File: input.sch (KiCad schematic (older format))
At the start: 15 parts

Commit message: Schematic finished
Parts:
- gave numbers to parts that had none: 15
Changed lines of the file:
@@
 LIBS:2450bl15b050
 LIBS:tlv4172
+LIBS:l4940d2t12-tr
+LIBS:tps54308
+LIBS:l78l33abu
+LIBS:adp150aujz-18
 LIBS:radar-cache
+LIBS:hn1c01fu
 EELAYER 25 0
 EELAYER END
 $Descr A4 11693 8268
 encoding utf-8
-Sheet 6 7
+Sheet 6 8
 Title ""
 Date ""
@@
 $EndDescr
 $Comp
-L 2500BP15M400 F?
+L 2500BP15M400 F601
 U 1 1 59D64427
 P 3330 3730
-F 0 "F?" H 3330 4180 60  0000 C CNN
+F 0 "F601" H 3330 4180 60  0000 C CNN
 F 1 "2500BP15M400" H 3830 3380 60  0000 C CNN
 F 2 "" H 3330 3730 60  0001 C CNN
@@
 $EndComp
 $Comp
-L taper T?
+L taper T601
 U 1 1 59D645E7
 P 2270 3730
-F 0 "T?" H 2270 3880 60  0000 C CNN
+F 0 "T601" H 2270 3880 60  0000 C CNN
 F 1 "taper" H 2170 3580 60  0000 C CNN
 F 2 "" H 2270 3730 60  0001 C CNN
@@
 $EndComp
 $Comp
-L GND #PWR?
+L GND #PWR056
 U 1 1 59D64760
 P 3360 4390
-F 0 "#PWR?" H 3360 4140 50  0001 C CNN
+F 0 "#PWR056" H 3360 4140 50  0001 C CNN
 F 1 "GND" H 3360 4240 50  0000 C CNN
 F 2 "" H 3360 4390 50  0001 C CNN
@@
 $EndComp
 $Comp
-L MGA-645T6 U?
+L MGA-645T6 U601
 U 1 1 59D64DB0
 P 5010 3730
-F 0 "U?" H 5010 4030 60  0000 C CNN
+F 0 "U601" H 5010 4030 60  0000 C CNN
 F 1 "MGA-645T6" H 5460 3380 60  0000 C CNN
 F 2 "" H 5010 3730 60  0001 C CNN
@@
 $EndComp
 $Comp
-L taper T?
+L taper T602
 U 1 1 59D651DD
 P 8520 3730
-F 0 "T?" H 8520 3880 60  0000 C CNN
+F 0 "T602" H 8520 3880 60  0000 C CNN
 F 1 "taper" H 8420 3580 60  0000 C CNN
 F 2 "" H 8520 3730 60  0001 C CNN
@@
 $EndComp
 $Comp
-L GND #PWR?
+L GND #PWR057
 U 1 1 59D653F1
 P 4910 4320
-F 0 "#PWR?" H 4910 4070 50  0001 C CNN
+F 0 "#PWR057" H 4910 4070 50  0001 C CNN
 F 1 "GND" H 4910 4170 50  0000 C CNN
 F 2 "" H 4910 4320 50  0001 C CNN
@@
 $EndComp
 $Comp
-L MGA-645T6 U?
+L MGA-645T6 U602
 U 1 1 59D659BC
 P 6900 3730
-F 0 "U?" H 6900 4030 60  0000 C CNN
+F 0 "U602" H 6900 4030 60  0000 C CNN
 F 1 "MGA-645T6" H 7350 3380 60  0000 C CNN
 F 2 "" H 6900 3730 60  0001 C CNN
@@
 $EndComp
 $Comp
-L GND #PWR?
+L GND #PWR058
 U 1 1 59D659C2
 P 6800 4320
-F 0 "#PWR?" H 6800 4070 50  0001 C CNN
+F 0 "#PWR058" H 6800 4070 50  0001 C CNN
 F 1 "GND" H 6800 4170 50  0000 C CNN
 F 2 "" H 6800 4320 50  0001 C CNN
@@
 RF_OUT
 $Comp
-L L_Small L?
+L L_Small L606
 U 1 1 59D6720C
 P 4240 4070
-F 0 "L?" H 4270 4110 50  0000 L CNN
+F 0 "L606" H 4270 4110 50  0000 L CNN
 F 1 "2.7n" H 4270 4030 50  0000 L CNN
 F 2 "" H 4240 4070 50  0001 C CNN
@@
 	2570 3730 2780 3730
 $Comp
-L L_Small L?
+L L_Small L605
 U 1 1 59D673E1
 P 6170 4050
-F 0 "L?" H 6200 4090 50  0000 L CNN
+F 0 "L605" H 6200 4090 50  0000 L CNN
 F 1 "2.7n" H 6200 4010 50  0000 L CNN
 F 2 "" H 6170 4050 50  0001 C CNN
@@
 $EndComp
 $Comp
-L L_Small L?
+L L_Small L603
 U 1 1 59D67473
 P 6020 3730
-F 0 "L?" H 6050 3770 50  0000 L CNN
+F 0 "L603" H 6050 3770 50  0000 L CNN
 F 1 "4.7n" H 6050 3690 50  0000 L CNN
 F 2 "" H 6020 3730 50  0001 C CNN
@@
 $EndComp
 $Comp
-L L_Small L?
+L L_Small L604
 U 1 1 59D67614
 P 7900 3730
-F 0 "L?" H 7930 3770 50  0000 L CNN
+F 0 "L604" H 7930 3770 50  0000 L CNN
 F 1 "4.7n" H 7930 3690 50  0000 L CNN
 F 2 "" H 7900 3730 50  0001 C CNN
@@
 Connection ~ 4240 3730
 $Comp
-L GND #PWR?
+L GND #PWR059
 U 1 1 59D67ABC
 P 4240 4360
-F 0 "#PWR?" H 4240 4110 50  0001 C CNN
+F 0 "#PWR059" H 4240 4110 50  0001 C CNN
 F 1 "GND" H 4240 4210 50  0000 C CNN
 F 2 "" H 4240 4360 50  0001 C CNN
@@
 	4240 4360 4240 4170
 $Comp
-L GND #PWR?
+L GND #PWR060
 U 1 1 59D67C59
 P 6170 4250
-F 0 "#PWR?" H 6170 4000 50  0001 C CNN
+F 0 "#PWR060" H 6170 4000 50  0001 C CNN
 F 1 "GND" H 6170 4100 50  0000 C CNN
 F 2 "" H 6170 4250 50  0001 C CNN
@@
 	6170 4150 6170 4250
 $Comp
-L +3V3 #PWR?
+L +3V3 #PWR061
 U 1 1 59D67FA5
 P 5210 2860
-F 0 "#PWR?" H 5210 2710 50  0001 C CNN
+F 0 "#PWR061" H 5210 2710 50  0001 C CNN
 F 1 "+3V3" H 5210 3000 50  0000 C CNN
 F 2 "" H 5210 2860 50  0001 C CNN
@@
 $EndComp
 $Comp
-L L_Small L?
+L L_Small L602
 U 1 1 59D67FDD
 P 5820 3220
-F 0 "L?" H 5850 3260 50  0000 L CNN
+F 0 "L602" H 5850 3260 50  0000 L CNN
 F 1 "3.9n" H 5850 3180 50  0000 L CNN
 F 2 "" H 5820 3220 50  0001 C CNN
@@
 $EndComp
 $Comp
-L L_Small L?
+L L_Small L601
 U 1 1 59D680B8
 P 7700 3210
-F 0 "L?" H 7730 3250 50  0000 L CNN
+F 0 "L601" H 7730 3250 50  0000 L CNN
 F 1 "3.9n" H 7730 3170 50  0000 L CNN
 F 2 "" H 7700 3210 50  0001 C CNN
@@
 	7700 3580 7700 3310
 $Comp
-L C_Small C?
+L C_Small C604
 U 1 1 59D6822A
 P 5450 3100
-F 0 "C?" H 5460 3170 50  0000 L CNN
+F 0 "C604" H 5460 3170 50  0000 L CNN
 F 1 "11p" H 5460 3020 50  0000 L CNN
 F 2 "" H 5450 3100 50  0001 C CNN
@@
 $EndComp
 $Comp
-L C_Small C?
+L C_Small C603
 U 1 1 59D68289
 P 5210 3100
-F 0 "C?" H 5220 3170 50  0000 L CNN
+F 0 "C603" H 5220 3170 50  0000 L CNN
 F 1 "0u1" H 5220 3020 50  0000 L CNN
 F 2 "" H 5210 3100 50  0001 C CNN
@@
 Connection ~ 5210 2910
 $Comp
-L +3V3 #PWR?
+L +3V3 #PWR062
 U 1 1 59D6867B
 P 7090 2830
-F 0 "#PWR?" H 7090 2680 50  0001 C CNN
+F 0 "#PWR062" H 7090 2680 50  0001 C CNN
 F 1 "+3V3" H 7090 2970 50  0000 C CNN
 F 2 "" H 7090 2830 50  0001 C CNN
@@
 $EndComp
 $Comp
-L C_Small C?
+L C_Small C602
 U 1 1 59D68681
 P 7330 3070
-F 0 "C?" H 7340 3140 50  0000 L CNN
+F 0 "C602" H 7340 3140 50  0000 L CNN
 F 1 "11p" H 7340 2990 50  0000 L CNN
 F 2 "" H 7330 3070 50  0001 C CNN
@@
 $EndComp
 $Comp
-L C_Small C?
+L C_Small C601
 U 1 1 59D68687
 P 7090 3070
-F 0 "C?" H 7100 3140 50  0000 L CNN
+F 0 "C601" H 7100 3140 50  0000 L CNN
 F 1 "0u1" H 7100 2990 50  0000 L CNN
 F 2 "" H 7090 3070 50  0001 C CNN
@@
 Connection ~ 5450 2910
 $Comp
-L GND #PWR?
+L GND #PWR063
 U 1 1 59D6874C
 P 5450 3270
-F 0 "#PWR?" H 5450 3020 50  0001 C CNN
+F 0 "#PWR063" H 5450 3020 50  0001 C CNN
 F 1 "GND" H 5450 3120 50  0000 C CNN
 F 2 "" H 5450 3270 50  0001 C CNN
@@
 $EndComp
 $Comp
-L GND #PWR?
+L GND #PWR064
 U 1 1 59D6878B
 P 7330 3270
-F 0 "#PWR?" H 7330 3020 50  0001 C CNN
+F 0 "#PWR064" H 7330 3020 50  0001 C CNN
 F 1 "GND" H 7330 3120 50  0000 C CNN
 F 2 "" H 7330 3270 50  0001 C CNN

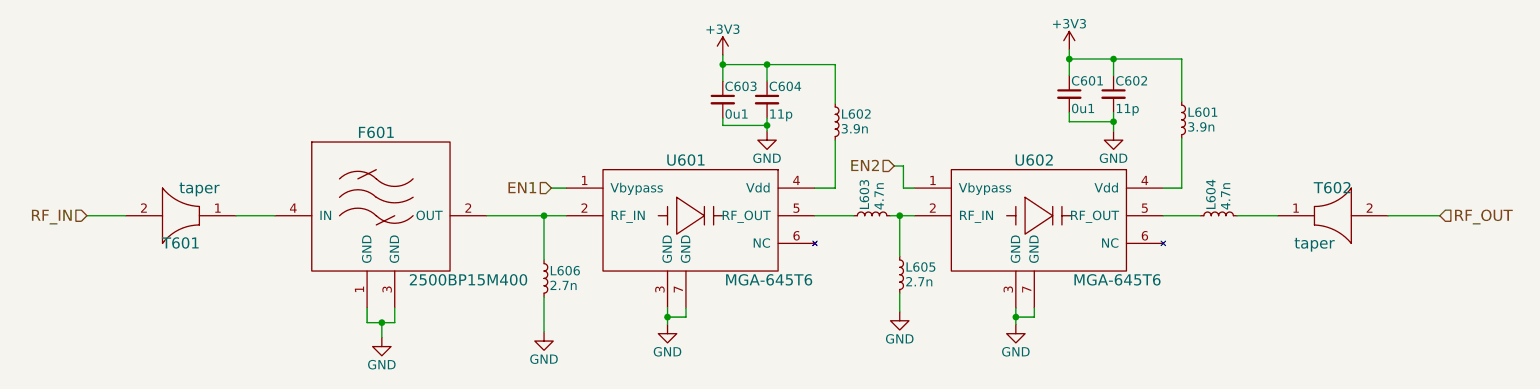
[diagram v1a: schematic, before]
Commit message: Assign a lot of footprints, fix l78l33abu part (input and output were reversed)
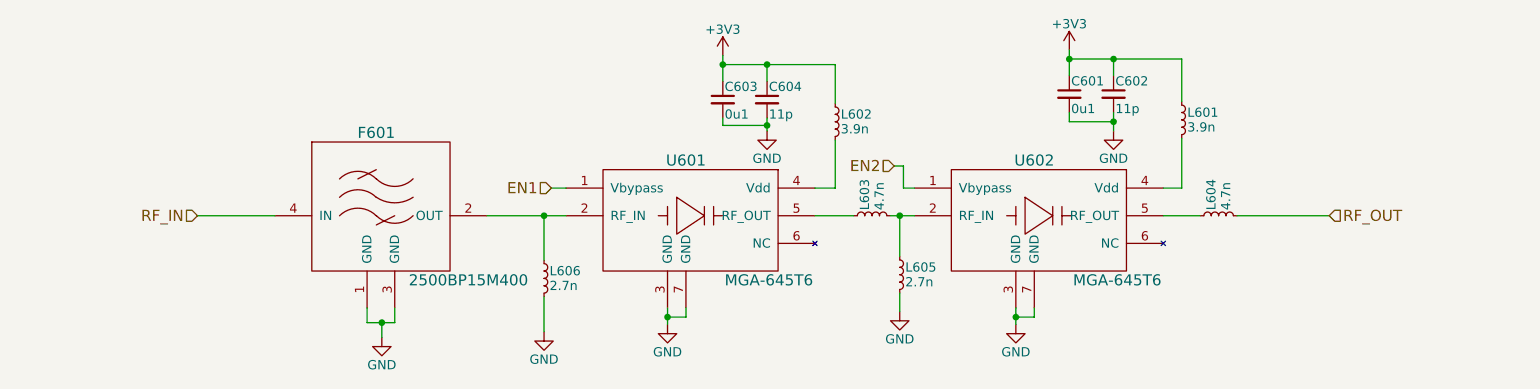
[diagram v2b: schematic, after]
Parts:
- removed T601, T602: taper, symbol taper
- C601, C603: footprint (none) -> Capacitors_SMD:C_0603_HandSoldering
- C602, C604, L601, L602, L603, L604, L605, L606: footprint (none) -> Capacitors_SMD:C_0402
- F601: footprint (none) -> rajsradar:2500BP15M400
- U601, U602: footprint (none) -> rajsradar:MGA-645T6
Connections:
- net RF_IN: now also F601.4 (IN)
- net RF_OUT: now also L604.2
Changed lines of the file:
@@
 F 0 "F601" H 3330 4180 60  0000 C CNN
 F 1 "2500BP15M400" H 3830 3380 60  0000 C CNN
-F 2 "" H 3330 3730 60  0001 C CNN
+F 2 "rajsradar:2500BP15M400" H 3330 3730 60  0001 C CNN
 F 3 "" H 3330 3730 60  0001 C CNN
 	1    3330 3730
@@
 $EndComp
 $Comp
-L taper T601
-U 1 1 59D645E7
-P 2270 3730
-F 0 "T601" H 2270 3880 60  0000 C CNN
-F 1 "taper" H 2170 3580 60  0000 C CNN
-F 2 "" H 2270 3730 60  0001 C CNN
-F 3 "" H 2270 3730 60  0001 C CNN
-	1    2270 3730
-	-1   0    0    1
-$EndComp
-$Comp
-L GND #PWR056
+L GND #PWR057
 U 1 1 59D64760
 P 3360 4390
-F 0 "#PWR056" H 3360 4140 50  0001 C CNN
+F 0 "#PWR057" H 3360 4140 50  0001 C CNN
 F 1 "GND" H 3360 4240 50  0000 C CNN
 F 2 "" H 3360 4390 50  0001 C CNN
@@
 F 0 "U601" H 5010 4030 60  0000 C CNN
 F 1 "MGA-645T6" H 5460 3380 60  0000 C CNN
-F 2 "" H 5010 3730 60  0001 C CNN
+F 2 "rajsradar:MGA-645T6" H 5010 3730 60  0001 C CNN
 F 3 "" H 5010 3730 60  0001 C CNN
 	1    5010 3730
@@
 $EndComp
 $Comp
-L taper T602
-U 1 1 59D651DD
-P 8520 3730
-F 0 "T602" H 8520 3880 60  0000 C CNN
-F 1 "taper" H 8420 3580 60  0000 C CNN
-F 2 "" H 8520 3730 60  0001 C CNN
-F 3 "" H 8520 3730 60  0001 C CNN
-	1    8520 3730
-	1    0    0    -1
-$EndComp
-$Comp
-L GND #PWR057
+L GND #PWR058
 U 1 1 59D653F1
 P 4910 4320
-F 0 "#PWR057" H 4910 4070 50  0001 C CNN
+F 0 "#PWR058" H 4910 4070 50  0001 C CNN
 F 1 "GND" H 4910 4170 50  0000 C CNN
 F 2 "" H 4910 4320 50  0001 C CNN
@@
 F 0 "U602" H 6900 4030 60  0000 C CNN
 F 1 "MGA-645T6" H 7350 3380 60  0000 C CNN
-F 2 "" H 6900 3730 60  0001 C CNN
+F 2 "rajsradar:MGA-645T6" H 6900 3730 60  0001 C CNN
 F 3 "" H 6900 3730 60  0001 C CNN
 	1    6900 3730
@@
 $EndComp
 $Comp
-L GND #PWR058
+L GND #PWR059
 U 1 1 59D659C2
 P 6800 4320
-F 0 "#PWR058" H 6800 4070 50  0001 C CNN
+F 0 "#PWR059" H 6800 4070 50  0001 C CNN
 F 1 "GND" H 6800 4170 50  0000 C CNN
 F 2 "" H 6800 4320 50  0001 C CNN
@@
 	1    0    0    -1
 $EndComp
-Text HLabel 1760 3730 0    60   Input ~ 0
+Text HLabel 2360 3730 0    60   Input ~ 0
 RF_IN
-Text HLabel 9100 3730 2    60   Input ~ 0
+Text HLabel 8500 3730 2    60   Input ~ 0
 RF_OUT
 $Comp
@@
 F 0 "L606" H 4270 4110 50  0000 L CNN
 F 1 "2.7n" H 4270 4030 50  0000 L CNN
-F 2 "" H 4240 4070 50  0001 C CNN
+F 2 "Capacitors_SMD:C_0402" H 4240 4070 50  0001 C CNN
 F 3 "" H 4240 4070 50  0001 C CNN
 	1    4240 4070
@@
 Connection ~ 6800 4280
 Wire Wire Line
-	9100 3730 8820 3730
-Wire Wire Line
-	1760 3730 1970 3730
-Wire Wire Line
-	2570 3730 2780 3730
+	8000 3730 8500 3730
+Wire Wire Line
+	2360 3730 2780 3730
 $Comp
 L L_Small L605
@@
 F 0 "L605" H 6200 4090 50  0000 L CNN
 F 1 "2.7n" H 6200 4010 50  0000 L CNN
-F 2 "" H 6170 4050 50  0001 C CNN
+F 2 "Capacitors_SMD:C_0402" H 6170 4050 50  0001 C CNN
 F 3 "" H 6170 4050 50  0001 C CNN
 	1    6170 4050
@@
 F 0 "L603" H 6050 3770 50  0000 L CNN
 F 1 "4.7n" H 6050 3690 50  0000 L CNN
-F 2 "" H 6020 3730 50  0001 C CNN
+F 2 "Capacitors_SMD:C_0402" H 6020 3730 50  0001 C CNN
 F 3 "" H 6020 3730 50  0001 C CNN
 	1    6020 3730
@@
 F 0 "L604" H 7930 3770 50  0000 L CNN
 F 1 "4.7n" H 7930 3690 50  0000 L CNN
-F 2 "" H 7900 3730 50  0001 C CNN
+F 2 "Capacitors_SMD:C_0402" H 7900 3730 50  0001 C CNN
 F 3 "" H 7900 3730 50  0001 C CNN
 	1    7900 3730
@@
 $EndComp
 Wire Wire Line
-	8000 3730 8220 3730
-Wire Wire Line
 	7800 3730 7600 3730
 Wire Wire Line
@@
 Connection ~ 4240 3730
 $Comp
-L GND #PWR059
+L GND #PWR060
 U 1 1 59D67ABC
 P 4240 4360
-F 0 "#PWR059" H 4240 4110 50  0001 C CNN
+F 0 "#PWR060" H 4240 4110 50  0001 C CNN
 F 1 "GND" H 4240 4210 50  0000 C CNN
 F 2 "" H 4240 4360 50  0001 C CNN
@@
 	4240 4360 4240 4170
 $Comp
-L GND #PWR060
+L GND #PWR061
 U 1 1 59D67C59
 P 6170 4250
-F 0 "#PWR060" H 6170 4000 50  0001 C CNN
+F 0 "#PWR061" H 6170 4000 50  0001 C CNN
 F 1 "GND" H 6170 4100 50  0000 C CNN
 F 2 "" H 6170 4250 50  0001 C CNN
@@
 	6170 4150 6170 4250
 $Comp
-L +3V3 #PWR061
+L +3V3 #PWR062
 U 1 1 59D67FA5
 P 5210 2860
-F 0 "#PWR061" H 5210 2710 50  0001 C CNN
+F 0 "#PWR062" H 5210 2710 50  0001 C CNN
 F 1 "+3V3" H 5210 3000 50  0000 C CNN
 F 2 "" H 5210 2860 50  0001 C CNN
@@
 F 0 "L602" H 5850 3260 50  0000 L CNN
 F 1 "3.9n" H 5850 3180 50  0000 L CNN
-F 2 "" H 5820 3220 50  0001 C CNN
+F 2 "Capacitors_SMD:C_0402" H 5820 3220 50  0001 C CNN
 F 3 "" H 5820 3220 50  0001 C CNN
 	1    5820 3220
@@
 F 0 "L601" H 7730 3250 50  0000 L CNN
 F 1 "3.9n" H 7730 3170 50  0000 L CNN
-F 2 "" H 7700 3210 50  0001 C CNN
+F 2 "Capacitors_SMD:C_0402" H 7700 3210 50  0001 C CNN
 F 3 "" H 7700 3210 50  0001 C CNN
 	1    7700 3210
@@
 F 0 "C604" H 5460 3170 50  0000 L CNN
 F 1 "11p" H 5460 3020 50  0000 L CNN
-F 2 "" H 5450 3100 50  0001 C CNN
+F 2 "Capacitors_SMD:C_0402" H 5450 3100 50  0001 C CNN
 F 3 "" H 5450 3100 50  0001 C CNN
 	1    5450 3100
@@
 F 0 "C603" H 5220 3170 50  0000 L CNN
 F 1 "0u1" H 5220 3020 50  0000 L CNN
-F 2 "" H 5210 3100 50  0001 C CNN
+F 2 "Capacitors_SMD:C_0603_HandSoldering" H 5210 3100 50  0001 C CNN
 F 3 "" H 5210 3100 50  0001 C CNN
 	1    5210 3100
@@
 Connection ~ 5210 2910
 $Comp
-L +3V3 #PWR062
+L +3V3 #PWR063
 U 1 1 59D6867B
 P 7090 2830
-F 0 "#PWR062" H 7090 2680 50  0001 C CNN
+F 0 "#PWR063" H 7090 2680 50  0001 C CNN
 F 1 "+3V3" H 7090 2970 50  0000 C CNN
 F 2 "" H 7090 2830 50  0001 C CNN
@@
 F 0 "C602" H 7340 3140 50  0000 L CNN
 F 1 "11p" H 7340 2990 50  0000 L CNN
-F 2 "" H 7330 3070 50  0001 C CNN
+F 2 "Capacitors_SMD:C_0402" H 7330 3070 50  0001 C CNN
 F 3 "" H 7330 3070 50  0001 C CNN
 	1    7330 3070
@@
 F 0 "C601" H 7100 3140 50  0000 L CNN
 F 1 "0u1" H 7100 2990 50  0000 L CNN
-F 2 "" H 7090 3070 50  0001 C CNN
+F 2 "Capacitors_SMD:C_0603_HandSoldering" H 7090 3070 50  0001 C CNN
 F 3 "" H 7090 3070 50  0001 C CNN
 	1    7090 3070
@@
 Connection ~ 5450 2910
 $Comp
-L GND #PWR063
+L GND #PWR064
 U 1 1 59D6874C
 P 5450 3270
-F 0 "#PWR063" H 5450 3020 50  0001 C CNN
+F 0 "#PWR064" H 5450 3020 50  0001 C CNN
 F 1 "GND" H 5450 3120 50  0000 C CNN
 F 2 "" H 5450 3270 50  0001 C CNN
@@
 $EndComp
 $Comp
-L GND #PWR064
+L GND #PWR065
 U 1 1 59D6878B
 P 7330 3270
-F 0 "#PWR064" H 7330 3020 50  0001 C CNN
+F 0 "#PWR065" H 7330 3020 50  0001 C CNN
 F 1 "GND" H 7330 3120 50  0000 C CNN
 F 2 "" H 7330 3270 50  0001 C CNN
